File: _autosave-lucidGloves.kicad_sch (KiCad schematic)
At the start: 25 parts, among them J1 USB_C_Receptacle_PowerOnly_6P, J10 Conn_01x05_Male, J11 Conn_01x05_Male, J12 Conn_01x19_Female, J13 Conn_01x05_Male, J14 Conn_01x03_Male, J15 Conn_01x03_Male, J16 Conn_01x03_Male, J17 Conn_01x03_Male, J18 Conn_01x03_Male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

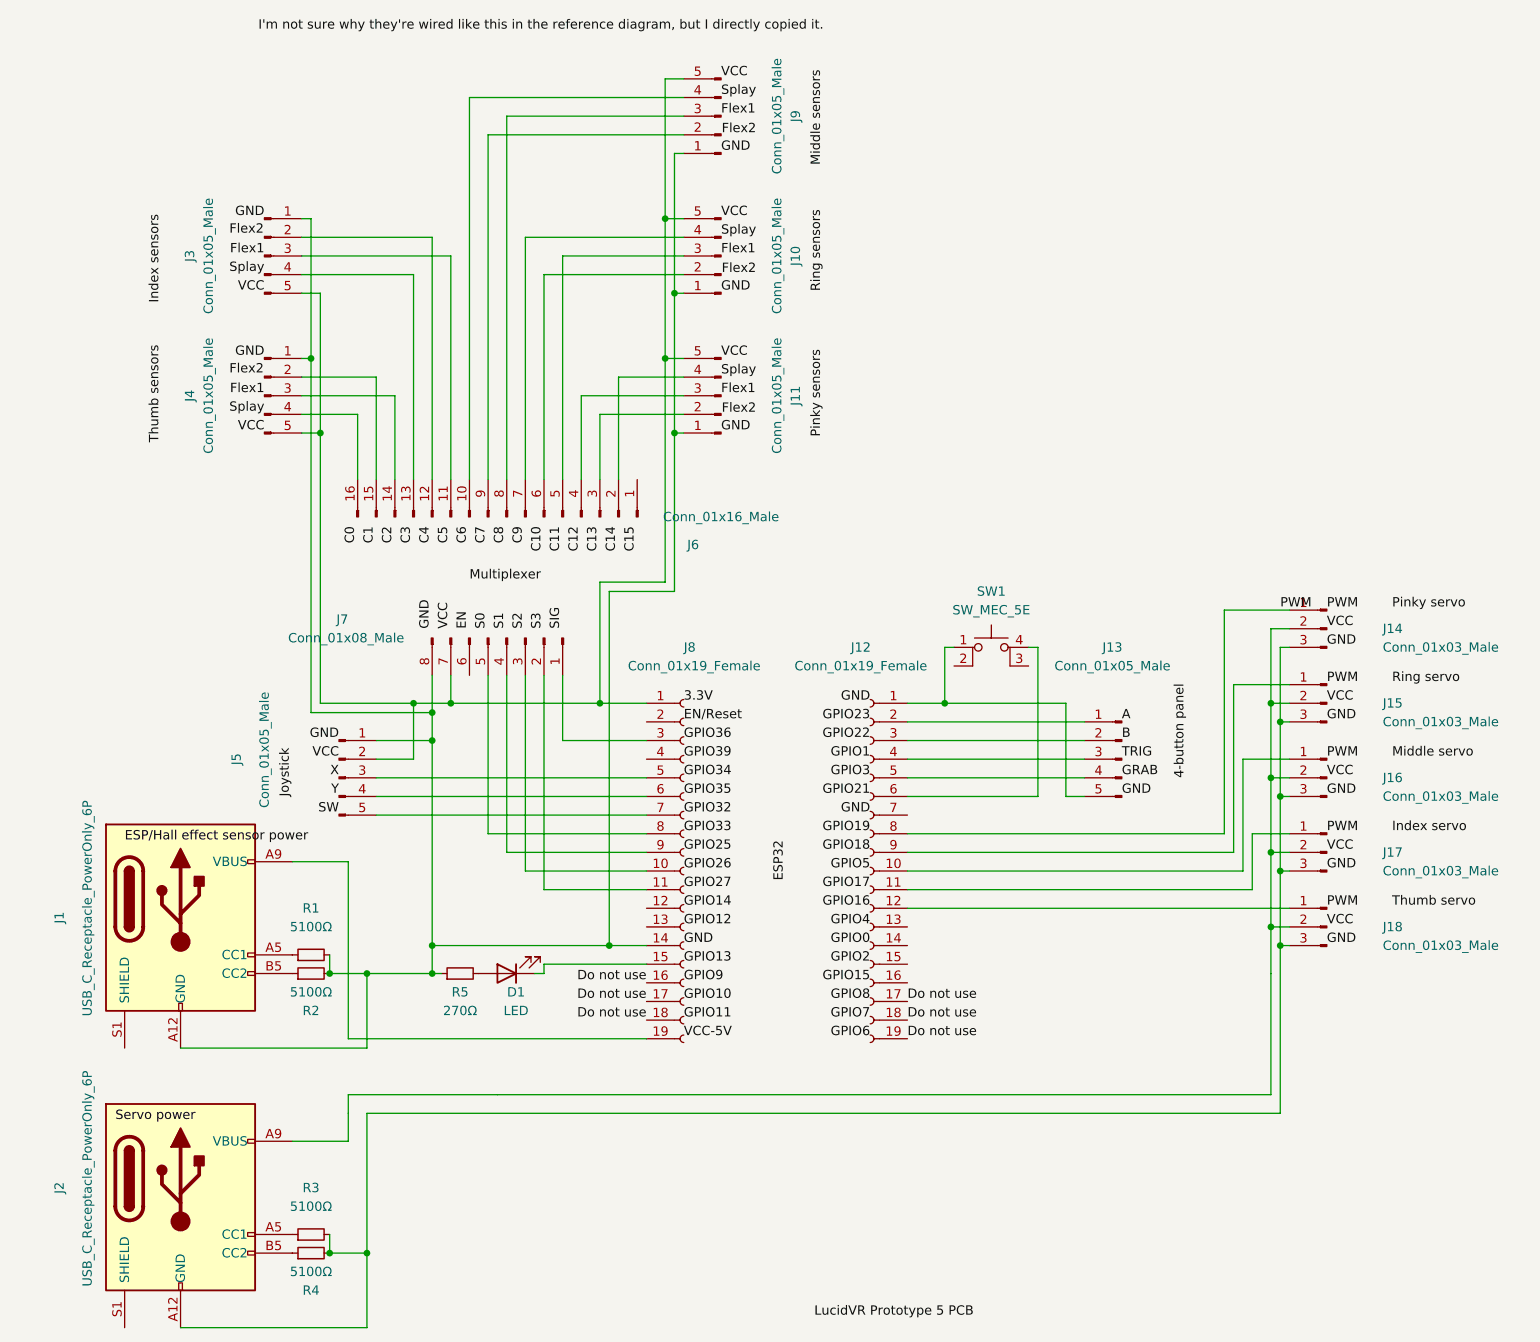
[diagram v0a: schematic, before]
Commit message: Change to KiCad 8, fix labels to be text elemnts
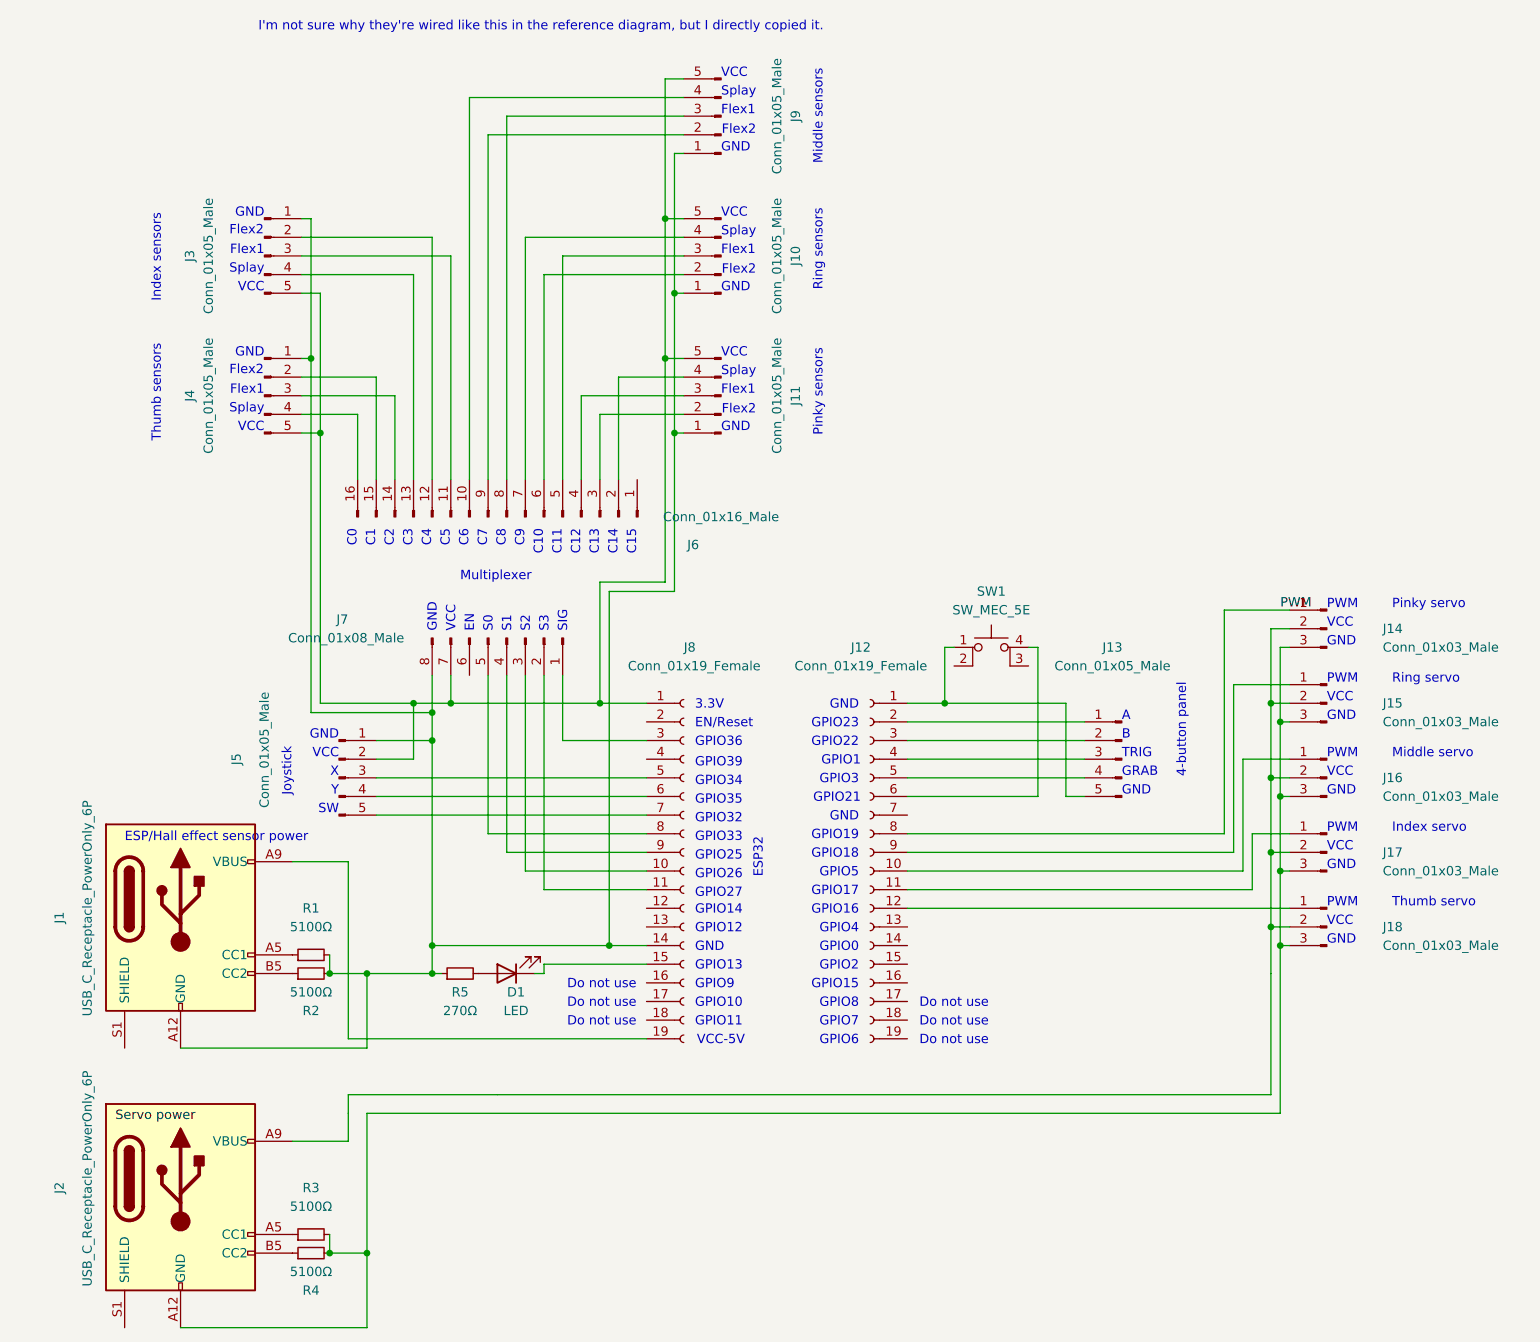
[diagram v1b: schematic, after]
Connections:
- removed net Do not use: J12.17 (Pin_17), J12.18 (Pin_18), J12.19 (Pin_19), J8.16 (Pin_16), J8.17 (Pin_17), J8.18 (Pin_18)
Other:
- note added: "3.3V"
- note added: "4-button panel"
- note added: "A"
- note added: "B"
- note added: "C0"
- note added: "C1"
- note added: "C10"
- note added: "C11"
- note added: "C12"
- note added: "C13"
- note added: "C14"
- note added: "C15"
- note added: "C2"
- note added: "C3"
- note added: "C4"
- note added: "C5"
- note added: "C6"
- note added: "C7"
- note added: "C8"
- note added: "C9"
- note added: "Do not use"
- note added: "EN"
- note added: "EN/Reset"
- note added: "ESP/Hall effect sensor power"
- note added: "ESP32"
- note added: "Flex1"
- note added: "Flex2"
- note added: "GND"
- note added: "GPIO0"
- note added: "GPIO1"
- note added: "GPIO10"
- note added: "GPIO11"
- note added: "GPIO12"
- note added: "GPIO13"
- note added: "GPIO14"
- note added: "GPIO15"
- note added: "GPIO16"
- note added: "GPIO17"
- note added: "GPIO18"
- note added: "GPIO19"
- note added: "GPIO2"
- note added: "GPIO21"
- note added: "GPIO22"
- note added: "GPIO23"
- note added: "GPIO25"
- note added: "GPIO26"
- note added: "GPIO27"
- note added: "GPIO3"
- note added: "GPIO32"
- note added: "GPIO33"
- note added: "GPIO34"
- note added: "GPIO35"
- note added: "GPIO36"
- note added: "GPIO39"
- note added: "GPIO4"
- note added: "GPIO5"
- note added: "GPIO6"
- note added: "GPIO7"
- note added: "GPIO8"
- note added: "GPIO9"
- note added: "GRAB"
- note added: "I'm not sure why they're wired like this in the reference diagram, but I directly copied it."
- note added: "Index sensors"
- note added: "Index servo"
- note added: "Joystick"
- note added: "Middle sensors"
- note added: "Middle servo"
- note added: "Multiplexer"
- note added: "PWM"
- note added: "Pinky sensors"
- note added: "Pinky servo"
- note added: "Ring sensors"
- note added: "Ring servo"
- note added: "S0"
- note added: "S1"
- note added: "S2"
- note added: "S3"
- note added: "SIG"
- note added: "SW"
- note added: "Splay"
- note added: "TRIG"
- note added: "Thumb sensors"
- note added: "Thumb servo"
- note added: "VCC"
- note added: "VCC-5V"
- note added: "X"
- note added: "Y"
- title: (none) -> LucidVR Prototype 5 PCB
